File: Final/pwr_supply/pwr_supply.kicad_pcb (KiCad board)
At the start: 2 copper layers, 28 parts, among them IC1 AP64350SP-13, IC2 AP64350SP-13, T1 Transformer_1P_SS

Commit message: 
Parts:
- added C13: 100n, Capacitor_SMD:C_1206_3216Metric_Pad1.33x1.80mm_HandSolder, F.Cu at (188.4, -52.0)
- added C14: 100n, Capacitor_SMD:C_1206_3216Metric_Pad1.33x1.80mm_HandSolder, F.Cu at (183.4, -39.0)
- C10, C9: footprint SamacSys_Parts:CAPC1608X90N -> Capacitor_SMD:C_1206_3216Metric_Pad1.33x1.80mm_HandSolder
- C11, C12: footprint SamacSys_Parts:CAPPRD225W50D680H1250 -> Capacitor_SMD:C_1206_3216Metric_Pad1.33x1.80mm_HandSolder
- C4, C8: footprint SamacSys_Parts:CAPC1005X56N -> Capacitor_SMD:C_1206_3216Metric_Pad1.33x1.80mm_HandSolder
- R5, R8: value 115k -> 309k
- RV1: footprint Varistor:RV_Disc_D15.5mm_W4.2mm_P7.5mm -> Varistor:RV_Disc_D16.5mm_W6.7mm_P7.5mm
- moved F1 396.8 mm to (26.0, -82.0)
- moved RV1 384.2 mm to (35.0, -50.0)
- moved C1 351.5 mm to (150.0, -94.0)
- moved C4 331.2 mm to (183.4, -94.0), turned to 180 degrees
- moved R1 331.0 mm to (166.8, -84.6)
- moved R3 319.4 mm to (184.8, -78.6)
- moved C7 313.7 mm to (152.8, -74.6), turned to 270 degrees
- moved IC1 311.8 mm to (173.2, -73.8)
- moved C10 310.0 mm to (178.4, -87.0), turned to 180 degrees
- moved L2 308.9 mm to (168.0, -63.0)
- moved R6 307.6 mm to (183.4, -59.0)
- moved C5 303.0 mm to (168.0, -54.0)
- moved T1 302.7 mm to (103.0, -52.0), turned to 270 degrees
- moved R5 301.7 mm to (194.0, -58.0)
- moved C8 297.4 mm to (164.4, -42.0)
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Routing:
- net Net-(C1-Pad1): track 0.00 -> 324.1 mm, vias 0 -> 8
- net Net-(C12-Pad1): track 0.00 -> 84.2 mm
- net Net-(C2-Pad1): track 0.00 -> 76.8 mm
- net Net-(C1-Pad2): track 0.00 -> 75.8 mm, vias 0 -> 2
- net Net-(F1-Pad2): track 0.00 -> 65.7 mm
- net Net-(C11-Pad1): track 0.00 -> 61.1 mm
- net Net-(C11-Pad2): track 0.00 -> 57.4 mm
- net Net-(D1-Pad2): track 0.00 -> 48.4 mm
- net Net-(C12-Pad2): track 0.00 -> 42.6 mm
- net Net-(RV1-Pad2): track 0.00 -> 37.3 mm
- net Net-(C8-Pad2): track 0.00 -> 33.1 mm
- net Net-(D1-Pad3): track 0.00 -> 29.4 mm
- net Net-(C9-Pad2): track 0.00 -> 27.3 mm
- net Net-(C4-Pad1): track 0.00 -> 26.3 mm
- net Net-(IC1-Pad4): track 0.00 -> 20.2 mm
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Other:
- board outline added: 200 x 100 mm
- board text added: "Designed by Andrew Henrikson"

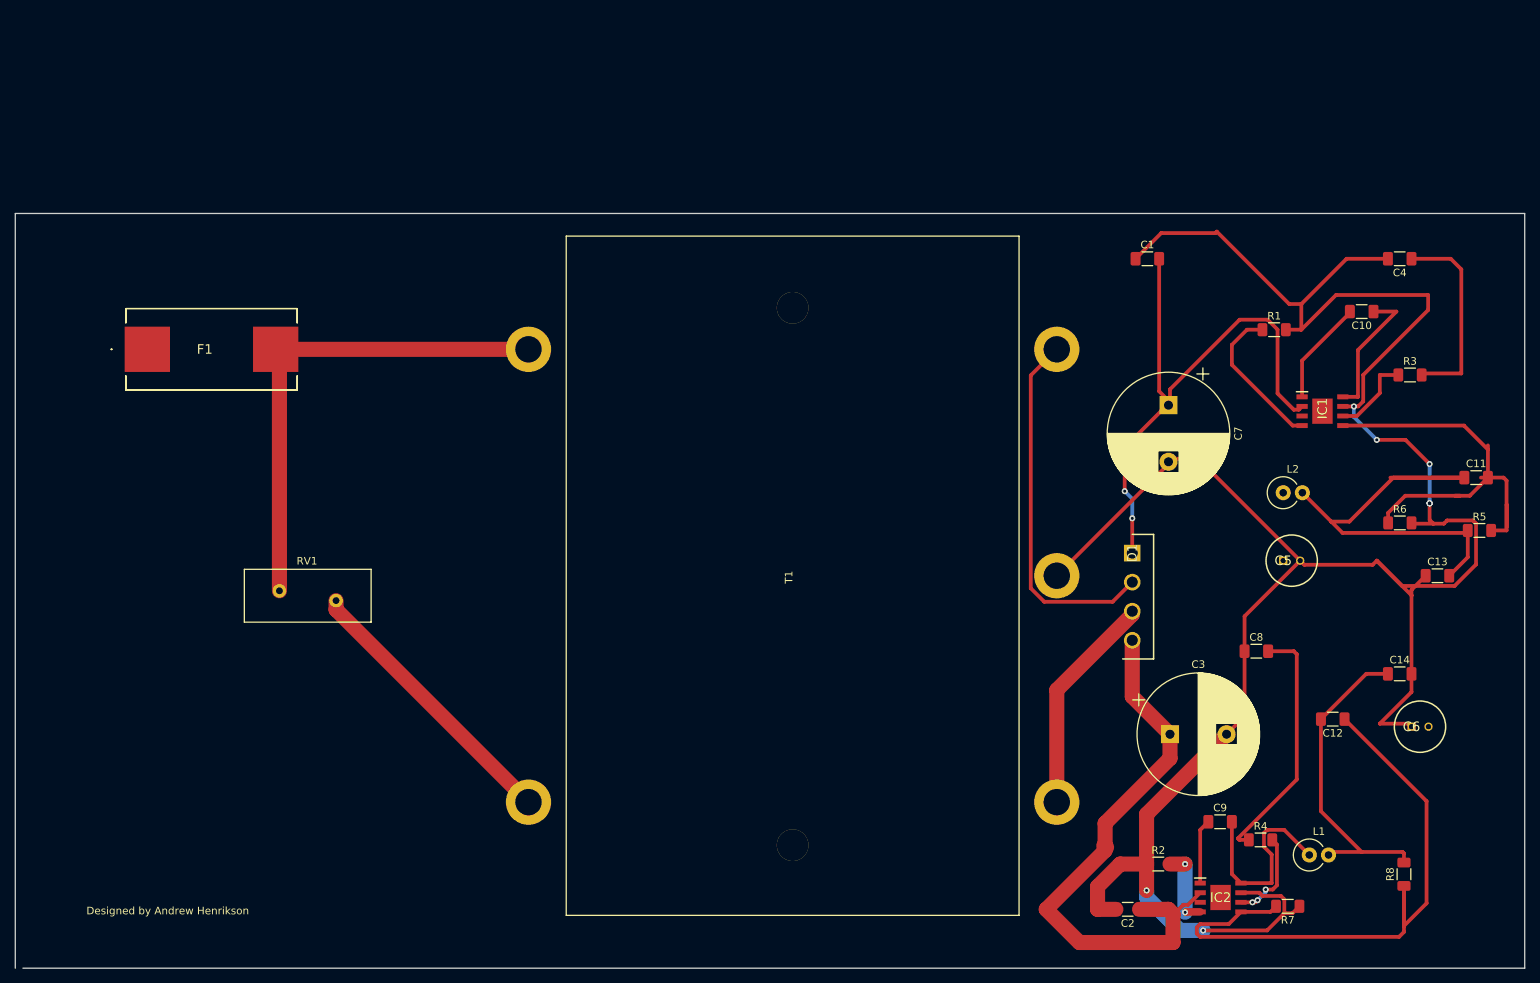
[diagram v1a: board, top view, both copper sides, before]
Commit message: 
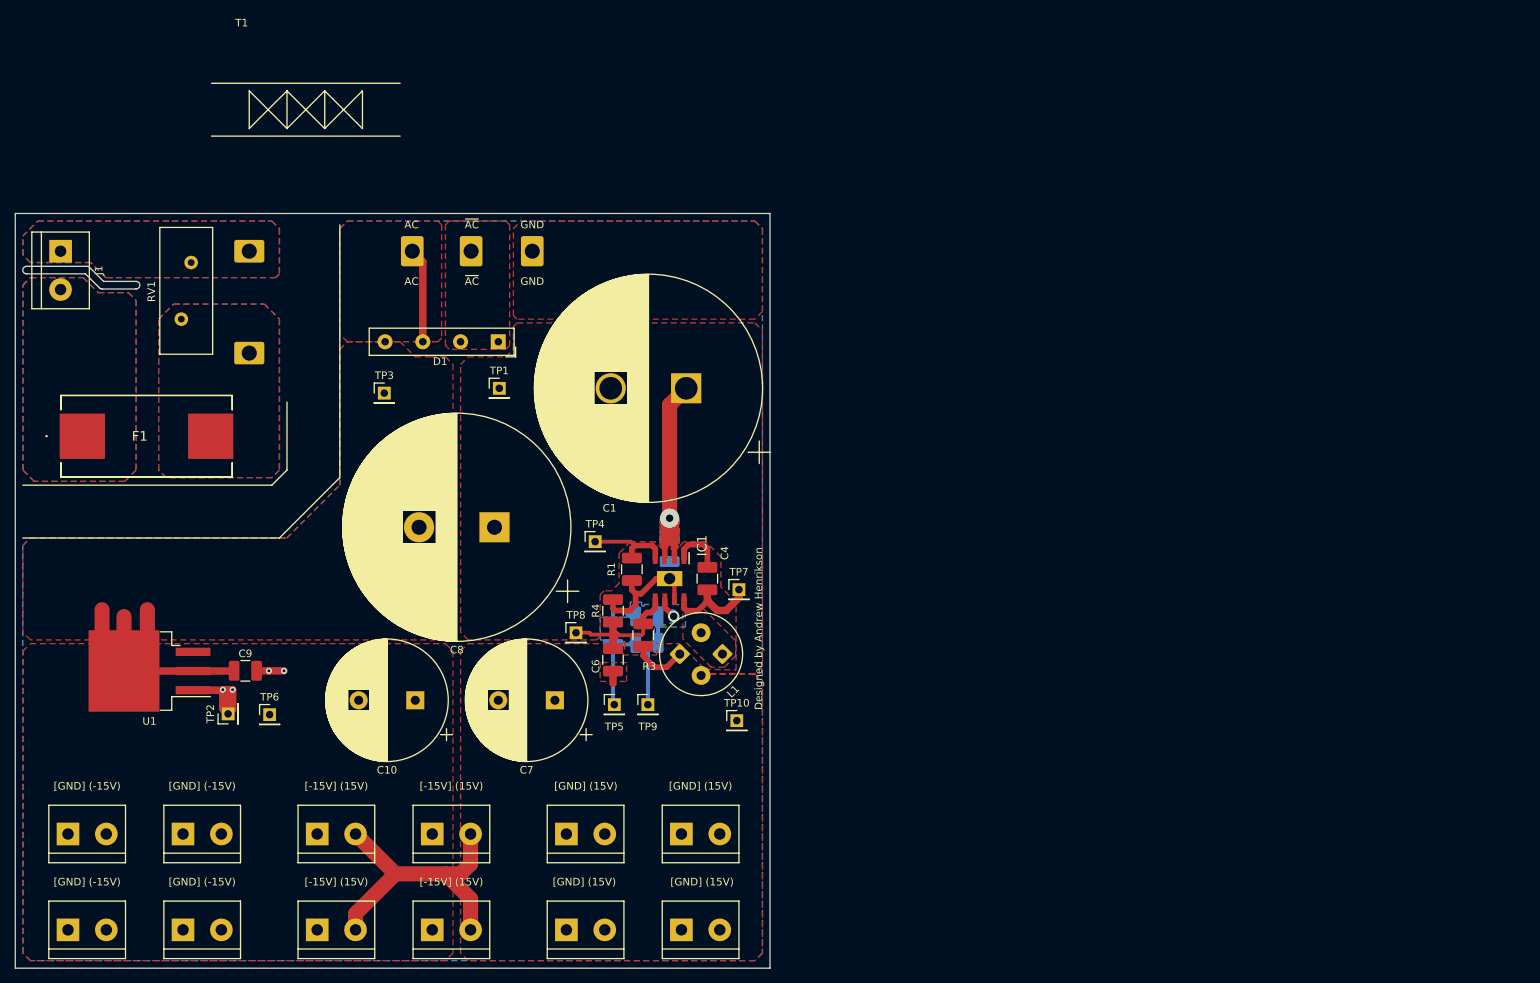
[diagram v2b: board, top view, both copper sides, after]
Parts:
- removed C11, C12: C_Small, Capacitor_SMD:C_1206_3216Metric_Pad1.33x1.80mm_HandSolder
- removed C13, C14: 100n, Capacitor_SMD:C_1206_3216Metric_Pad1.33x1.80mm_HandSolder
- removed IC2: AP64350SP-13, SOIC127P600X163-9N
- removed L2: 200u, Inductor_THT:L_Axial_L9.5mm_D4.0mm_P2.54mm_Vertical_Fastron_SMCC
- removed R5, R8: 309k, Resistor_SMD:R_1206_3216Metric_Pad1.30x1.75mm_HandSolder
- removed R6, R7: 22.1k, Resistor_SMD:R_1206_3216Metric_Pad1.30x1.75mm_HandSolder
- added J1: Screw_Terminal_01x02, TerminalBlock:TerminalBlock_bornier-2_P5.08mm, F.Cu at (6.00, -95.0)
- added J10: Screw_Terminal_01x02, TerminalBlock:TerminalBlock_bornier-2_P5.08mm, F.Cu at (55.2, -17.8)
- added J11: Screw_Terminal_01x02, TerminalBlock:TerminalBlock_bornier-2_P5.08mm, F.Cu at (73.0, -17.8)
- added J12: Screw_Terminal_01x02, TerminalBlock:TerminalBlock_bornier-2_P5.08mm, F.Cu at (6.99, -17.8)
- added J13: Screw_Terminal_01x02, TerminalBlock:TerminalBlock_bornier-2_P5.08mm, F.Cu at (40.0, -5.08)
- added J2: Screw_Terminal_01x02, TerminalBlock:TerminalBlock_bornier-2_P5.08mm, F.Cu at (88.3, -5.08)
- added J3: Screw_Terminal_01x02, TerminalBlock:TerminalBlock_bornier-2_P5.08mm, F.Cu at (22.2, -17.8)
- added J4: Screw_Terminal_01x02, TerminalBlock:TerminalBlock_bornier-2_P5.08mm, F.Cu at (40.0, -17.8)
- added J5: Screw_Terminal_01x02, TerminalBlock:TerminalBlock_bornier-2_P5.08mm, F.Cu at (88.3, -17.8)
- added J6: Screw_Terminal_01x02, TerminalBlock:TerminalBlock_bornier-2_P5.08mm, F.Cu at (22.2, -5.08)
- added J7: Screw_Terminal_01x02, TerminalBlock:TerminalBlock_bornier-2_P5.08mm, F.Cu at (55.2, -5.08)
- added J8: Screw_Terminal_01x02, TerminalBlock:TerminalBlock_bornier-2_P5.08mm, F.Cu at (73.0, -5.08)
- added J9: Screw_Terminal_01x02, TerminalBlock:TerminalBlock_bornier-2_P5.08mm, F.Cu at (6.99, -5.08)
- added TP1: TestPoint, Connector_PinHeader_2.54mm:PinHeader_1x01_P2.54mm_Vertical, F.Cu at (64.1, -76.8)
- added TP10: TestPoint, Connector_PinHeader_2.54mm:PinHeader_1x01_P2.54mm_Vertical, F.Cu at (95.6, -32.8)
- added TP2: TestPoint, Connector_PinHeader_2.54mm:PinHeader_1x01_P2.54mm_Vertical, F.Cu at (28.2, -33.7)
- added TP3: TestPoint, Connector_PinHeader_2.54mm:PinHeader_1x01_P2.54mm_Vertical, F.Cu at (48.9, -76.2)
- added TP4: TestPoint, Connector_PinHeader_2.54mm:PinHeader_1x01_P2.54mm_Vertical, F.Cu at (76.8, -56.5)
- added TP5: TestPoint, Connector_PinHeader_2.54mm:PinHeader_1x01_P2.54mm_Vertical, F.Cu at (79.4, -34.9)
- added TP6: TestPoint, Connector_PinHeader_2.54mm:PinHeader_1x01_P2.54mm_Vertical, F.Cu at (33.7, -33.6)
- added TP7: TestPoint, Connector_PinHeader_2.54mm:PinHeader_1x01_P2.54mm_Vertical, F.Cu at (95.9, -50.2)
- added TP8: TestPoint, Connector_PinHeader_2.54mm:PinHeader_1x01_P2.54mm_Vertical, F.Cu at (74.3, -44.5)
- added TP9: TestPoint, Connector_PinHeader_2.54mm:PinHeader_1x01_P2.54mm_Vertical, F.Cu at (83.8, -34.9)
- added U1: 926-LM2990SX-15/NOPB, Package_TO_SOT_SMD:TO-263-3_TabPin2, F.Cu at (17.8, -39.4)
- C1: value 2.2u -> 8200uF; footprint Capacitor_SMD:C_1206_3216Metric_Pad1.33x1.80mm_HandSolder -> Capacitor_THT:CP_Radial_D30.0mm_P10.00mm_SnapIn
- C10: value 100n -> 1000u; footprint Capacitor_SMD:C_1206_3216Metric_Pad1.33x1.80mm_HandSolder -> Capacitor_THT:CP_Radial_D16.0mm_P7.50mm
- C2: footprint Capacitor_SMD:C_1206_3216Metric_Pad1.33x1.80mm_HandSolder -> Capacitor_SMD:C_1210_3225Metric_Pad1.42x2.65mm_HandSolder; moved to B.Cu
- C3: value 1000u -> 3.3n; footprint Capacitor_THT:CP_Radial_D16.0mm_P7.50mm -> Capacitor_SMD:C_1210_3225Metric_Pad1.42x2.65mm_HandSolder; moved to B.Cu
- C4: value 3.3n -> 100n; footprint Capacitor_SMD:C_1206_3216Metric_Pad1.33x1.80mm_HandSolder -> Capacitor_SMD:C_1210_3225Metric_Pad1.42x2.65mm_HandSolder
- C5: value 100u -> OPEN; footprint SamacSys_Parts:CAPPRD225W50D680H1250 -> Capacitor_SMD:C_1210_3225Metric_Pad1.42x2.65mm_HandSolder; moved to B.Cu
- C6: value 100u -> OPEN; footprint SamacSys_Parts:CAPPRD225W50D680H1250 -> Capacitor_SMD:C_1210_3225Metric_Pad1.42x2.65mm_HandSolder
- C8: value 3.3n -> 8200uF; footprint Capacitor_SMD:C_1206_3216Metric_Pad1.33x1.80mm_HandSolder -> Capacitor_THT:CP_Radial_D30.0mm_P10.00mm_SnapIn
- C9: value 100n -> 2.2u; footprint Capacitor_SMD:C_1206_3216Metric_Pad1.33x1.80mm_HandSolder -> Capacitor_SMD:C_1210_3225Metric_Pad1.42x2.65mm_HandSolder
- D1: footprint SamacSys_Parts:TO385P410X1600X1290-4P -> Diode_THT:Diode_Bridge_19.0x3.5x10.0mm_P5.0mm
- IC1: value AP64350SP-13 -> AP64350SP-13_alt
- L1: value 200u -> 33u; footprint Inductor_THT:L_Axial_L9.5mm_D4.0mm_P2.54mm_Vertical_Fastron_SMCC -> SamacSys_Parts:12RS333C
- R1: footprint Resistor_SMD:R_1206_3216Metric_Pad1.30x1.75mm_HandSolder -> Capacitor_SMD:C_1210_3225Metric_Pad1.42x2.65mm_HandSolder
- R2: value 220k -> 14k; footprint Resistor_SMD:R_1206_3216Metric_Pad1.30x1.75mm_HandSolder -> Capacitor_SMD:C_1210_3225Metric_Pad1.42x2.65mm_HandSolder; moved to B.Cu
- R3: value 14k -> 17.8k; footprint Resistor_SMD:R_1206_3216Metric_Pad1.30x1.75mm_HandSolder -> Capacitor_SMD:C_1210_3225Metric_Pad1.42x2.65mm_HandSolder
- R4: value 14k -> 1k; footprint Resistor_SMD:R_1206_3216Metric_Pad1.30x1.75mm_HandSolder -> Capacitor_SMD:C_1210_3225Metric_Pad1.42x2.65mm_HandSolder
- T1: value Transformer_1P_SS -> 120rms:28rms 3.6A; footprint SamacSys_Parts:241-6-24 -> SamacSys_Parts:Transformer_Entry
- moved C10 135.6 mm to (53.0, -35.5)
- moved C9 130.7 mm to (30.5, -39.4)
- moved R3 107.3 mm to (83.2, -44.1), turned to 90 degrees
- moved C6 106.2 mm to (79.2, -40.9), turned to 90 degrees
- moved C8 102.3 mm to (63.5, -58.4), turned to 180 degrees
- moved C4 101.1 mm to (91.7, -51.6), turned to 90 degrees
- moved T1 99.9 mm to (31.0, -121.2), turned to 0 degrees
- moved R4 91.0 mm to (79.2, -47.4), turned to 90 degrees
- moved R1 90.8 mm to (81.7, -52.9), turned to 270 degrees
- moved C7 90.2 mm to (71.5, -35.5), turned to 180 degrees
- moved IC1 89.3 mm to (86.7, -51.6), turned to 270 degrees
- moved D1 88.5 mm to (64.0, -83.0), turned to 180 degrees
- moved C5 84.6 mm to (83.7, -46.6), turned to 180 degrees
- moved L1 82.2 mm to (93.7, -41.6), turned to 225 degrees
- moved C2 77.1 mm to (86.7, -55.4), turned to 90 degrees
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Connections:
- net Net-(D1-Pad2) renamed /lowside_ac_1
- net Net-(D1-Pad3) renamed /lowside_ac_2
- C1 pad 1: Net-(C1-Pad1) -> /rect_ac_+
- C1 pad 2: Net-(C1-Pad2) -> GND
- C10 pad 1: Net-(C10-Pad1) -> GND
- C10 pad 2: Net-(C10-Pad2) -> -15VDC
- C2 pad 1: Net-(C2-Pad1) -> GND
- C2 pad 2: Net-(C1-Pad1) -> /rect_ac_+
- C3 pad 1: Net-(C2-Pad1) -> Net-(C3-Pad1)
- C3 pad 2: Net-(C1-Pad1) -> GND
- C4 pad 2: Net-(C1-Pad1) -> Net-(C4-Pad2)
- C5 pad 2: Net-(C1-Pad1) -> GND
- C6 pad 1: Net-(C1-Pad1) -> 15VDC
- C7 pad 1: Net-(C1-Pad2) -> 15VDC
- C7 pad 2: Net-(C1-Pad1) -> GND
- C8 pad 1: Net-(C1-Pad1) -> GND
- C8 pad 2: Net-(C8-Pad2) -> /rect_ac_-
- C9 pad 1: Net-(C9-Pad1) -> /rect_ac_-
- C9 pad 2: Net-(C9-Pad2) -> GND
- D1 pad 1: Net-(C1-Pad2) -> /rect_ac_+
- D1 pad 4: Net-(C2-Pad1) -> /rect_ac_-
- IC1 pad 1: Net-(C10-Pad2) -> Net-(C4-Pad2)
- IC1 pad 2: Net-(C1-Pad2) -> /rect_ac_+
- IC1 pad 3: Net-(C1-Pad2) -> /rect_ac_+
- IC1 pad 5: Net-(C11-Pad2) -> Net-(C6-Pad2)
- IC1 pad 6: Net-(IC1-Pad6) -> Net-(C5-Pad1)
- IC1 pad 7: Net-(C1-Pad1) -> GND
- IC1 pad 8: Net-(C10-Pad1) -> Net-(C4-Pad1)
- IC1 pad 9: Net-(IC1-Pad9) -> GND
- L1 pad 1: Net-(C9-Pad2) -> Net-(C4-Pad1)
- L1 pad 2: Net-(C12-Pad2) -> 15VDC
- R1 pad 2: Net-(C1-Pad1) -> GND
- R2 pad 1: Net-(C1-Pad1) -> Net-(C5-Pad1)
- R2 pad 2: Net-(IC2-Pad4) -> Net-(C3-Pad1)
- R3 pad 1: Net-(IC1-Pad6) -> 15VDC
- R3 pad 2: Net-(C4-Pad1) -> Net-(C6-Pad2)
- R4 pad 1: Net-(C8-Pad2) -> Net-(C6-Pad2)
- R4 pad 2: Net-(IC2-Pad6) -> GND
- T1 pad 4: Net-(C1-Pad1) -> GND
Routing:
- net Net-(C1-Pad1): track 324.1 -> 0.00 mm, vias 8 -> 0
- net Net-(C12-Pad1): track 84.2 -> 0.00 mm
- net Net-(C2-Pad1): track 76.8 -> 0.00 mm
- net Net-(C1-Pad2): track 75.8 -> 0.00 mm, vias 2 -> 0
- net Net-(F1-Pad2): track 65.7 -> 0.00 mm
- net Net-(C11-Pad1): track 61.1 -> 0.00 mm
- net Net-(C11-Pad2): track 57.4 -> 0.00 mm
- net 15VDC: track 0.00 -> 49.5 mm
- net /lowside_ac_1: track 48.4 -> 0.00 mm
- net Net-(C12-Pad2): track 42.6 -> 0.00 mm
- net /rect_ac_-: track 0.00 -> 40.6 mm
- net GND: track 0.00 -> 40.3 mm, vias 0 -> 4
- net Net-(J1-Pad1): track 37.3 -> 0.00 mm
- net Net-(C8-Pad2): track 33.1 -> 0.00 mm
- net /rect_ac_+: track 0.00 -> 30.9 mm, vias 0 -> 1
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- added copper zone on F.Cu, net -15VDC
- added copper zone on F.Cu, net /lowside_ac_1
- added copper zone on F.Cu, net /lowside_ac_2
- added copper zone on B.Cu, net /rect_ac_+
- added copper zone on F.Cu, net /rect_ac_+
- added copper zone on F.Cu, net /rect_ac_-
- added copper zone on F.Cu, net 15VDC
- added copper zone on B.Cu, net GND
- added copper zone on F.Cu, net GND
- added copper zone on F.Cu, net Net-(C4-Pad1)
- added copper zone on B.Cu, net Net-(C5-Pad1)
- added copper zone on B.Cu, net Net-(F1-Pad1)
- added copper zone on F.Cu, net Net-(F1-Pad1)
- added copper zone on B.Cu, net Net-(F1-Pad2)
- added copper zone on F.Cu, net Net-(F1-Pad2)
- added copper zone on B.Cu, net Net-(J1-Pad1)
- added copper zone on F.Cu, net Net-(J1-Pad1)
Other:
- board size 200 x 100 mm -> 100 x 100 mm
- rule trace_min: 0.2 -> 0.5
- board text added: "AC"
- board text added: "GND"
- board text added: "[-15V] (15V)"
- board text added: "[GND] (-15V)"
- board text added: "[GND] (15V)"
- board text added: "~AC"
